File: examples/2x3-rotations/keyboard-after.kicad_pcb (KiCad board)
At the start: 2 copper layers, 8 parts, among them SW1 SW_Push, SW2 SW_Push, SW3 SW_Push, SW4 SW_Push

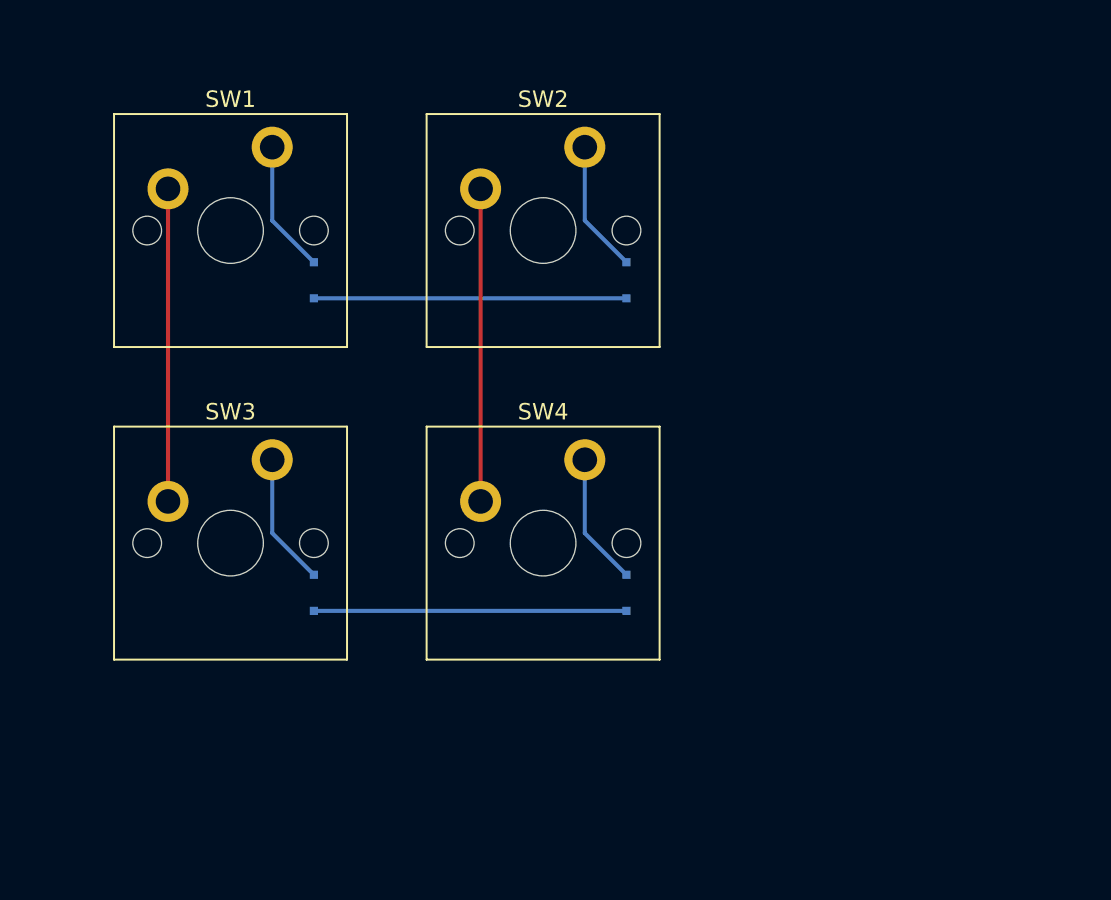
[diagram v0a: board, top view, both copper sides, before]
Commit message: examples result update
also simplified example filenames and add new example
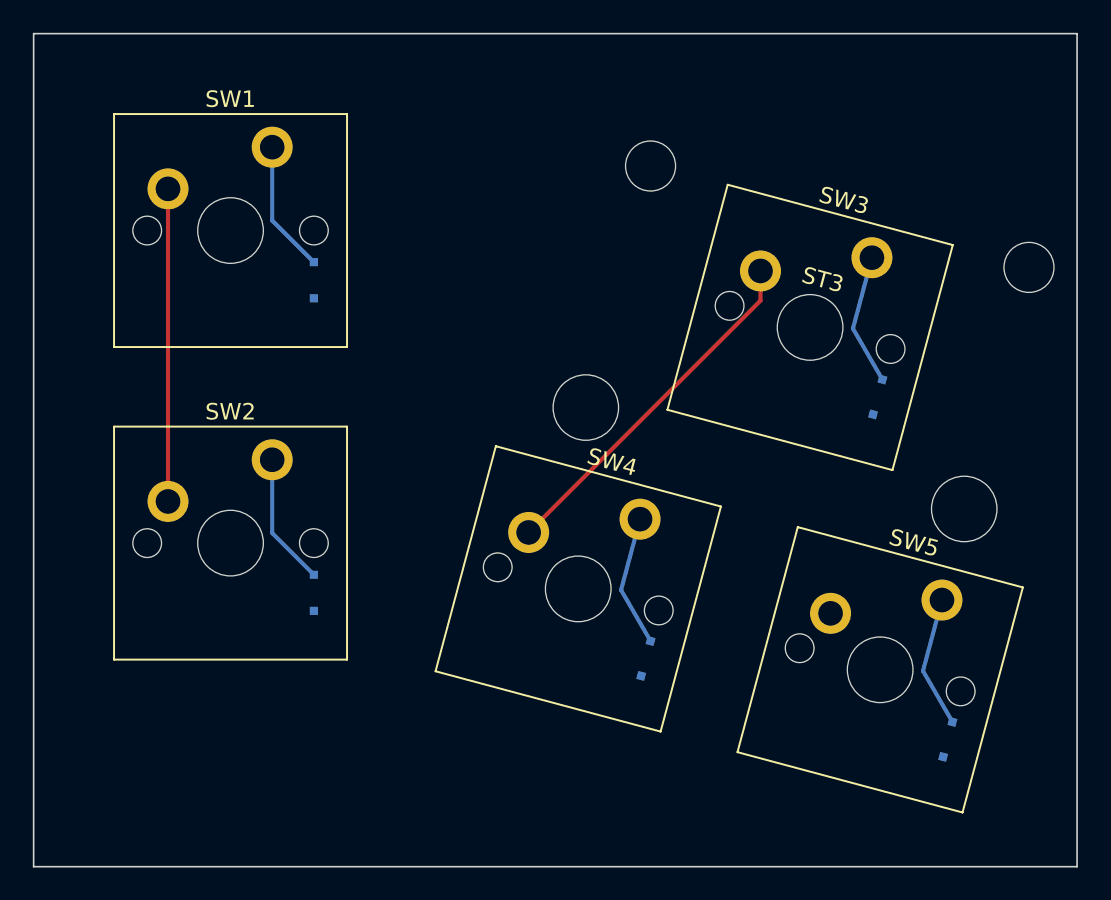
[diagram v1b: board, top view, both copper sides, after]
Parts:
- added D5: D, Diode_SMD:D_SOD-323F, B.Cu at (78.2, 65.5)
- added ST3: MountingHole, Mounting_Keyboard_Stabilizer:Stabilizer_Cherry_MX_2u, F.Cu at (69.8, 40.4)
- added SW5: SW_Push, Switch_Keyboard_Cherry_MX:SW_Cherry_MX_PCB_1.00u, F.Cu at (74.1, 61.3)
- SW3: footprint Switch_Keyboard_Cherry_MX:SW_Cherry_MX_PCB_1.00u -> Switch_Keyboard_Cherry_MX:SW_Cherry_MX_PCB_2.00u
- moved SW3 37.7 mm to (69.8, 40.4), turned to 345 degrees
- moved D3 36.4 mm to (74.0, 44.7), turned to 75 degrees
- moved SW2 26.9 mm to (34.5, 53.6)
- moved D2 26.9 mm to (39.6, 56.6)
- moved D4 4.17 mm to (59.8, 60.6), turned to 75 degrees
- moved SW4 3.52 mm to (55.7, 56.4), turned to 345 degrees
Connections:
- D2 pad 1: ROW0 -> ROW1
- D3 pad 1: ROW1 -> ROW0
- SW2 pad 1: COL1 -> COL0
- SW3 pad 1: COL0 -> COL1
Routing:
- net ROW1: track 19.1 -> 0.00 mm
- net ROW0: track 19.1 -> 0.00 mm
- net N$5: track 0.00 -> 8.06 mm
- net COL1: track 19.0 -> 21.8 mm
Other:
- board outline added: 63.6 x 50.8 mm

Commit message: Update examples kicad files
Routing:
- net COL1: track 21.8 -> 0.00 mm
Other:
- board outline removed
- net class Default removed

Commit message: Maintain own copy of footprints used in examples
Because testing with more footprints variants will be added soon,
it would be easier to maintain own copy of used footprints than
include multiple submodules for various libraries.
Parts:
- ST3: footprint Mounting_Keyboard_Stabilizer:Stabilizer_Cherry_MX_2u -> examples:Stabilizer_Cherry_MX_2u
- SW1, SW2, SW4, SW5: footprint Switch_Keyboard_Cherry_MX:SW_Cherry_MX_PCB_1.00u -> examples:SW_Cherry_MX_PCB_1.00u
- SW3: footprint Switch_Keyboard_Cherry_MX:SW_Cherry_MX_PCB_2.00u -> examples:SW_Cherry_MX_PCB_2.00u
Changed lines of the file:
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@@
   (net 9 "ROW0")
   (net 10 "ROW1")
-  (footprint "Mounting_Keyboard_Stabilizer:Stabilizer_Cherry_MX_2u" (layer "F.Cu")
+  (footprint "examples:Stabilizer_Cherry_MX_2u" (layer "F.Cu")
     (at 69.846641 40.429172 -15)
     (descr "Cherry MX key stabilizer 2u 2.25u 2.5u 2.75u")
@@
     )
   )
-  (footprint "Switch_Keyboard_Cherry_MX:SW_Cherry_MX_PCB_1.00u" (layer "F.Cu")
+  (footprint "examples:SW_Cherry_MX_PCB_1.00u" (layer "F.Cu")
     (at 34.525 34.525)
     (descr "Cherry MX keyswitch, https://www.cherrymx.de/en/dev.html")
@@
     )
   )
-  (footprint "Switch_Keyboard_Cherry_MX:SW_Cherry_MX_PCB_1.00u" (layer "F.Cu")
+  (footprint "examples:SW_Cherry_MX_PCB_1.00u" (layer "F.Cu")
     (at 34.525 53.575)
     (descr "Cherry MX keyswitch, https://www.cherrymx.de/en/dev.html")
@@
     )
   )
-  (footprint "Switch_Keyboard_Cherry_MX:SW_Cherry_MX_PCB_2.00u" (layer "F.Cu")
+  (footprint "examples:SW_Cherry_MX_PCB_2.00u" (layer "F.Cu")
     (at 69.846641 40.429172 -15)
     (descr "Cherry MX keyswitch, https://www.cherrymx.de/en/dev.html")
@@
     )
   )
-  (footprint "Switch_Keyboard_Cherry_MX:SW_Cherry_MX_PCB_1.00u" (layer "F.Cu")
+  (footprint "examples:SW_Cherry_MX_PCB_1.00u" (layer "F.Cu")
     (at 55.715695 56.364808 -15)
     (descr "Cherry MX keyswitch, https://www.cherrymx.de/en/dev.html")
@@
     )
   )
-  (footprint "Switch_Keyboard_Cherry_MX:SW_Cherry_MX_PCB_1.00u" (layer "F.Cu")
+  (footprint "examples:SW_Cherry_MX_PCB_1.00u" (layer "F.Cu")
     (at 74.116582 61.295311 -15)
     (descr "Cherry MX keyswitch, https://www.cherrymx.de/en/dev.html")
